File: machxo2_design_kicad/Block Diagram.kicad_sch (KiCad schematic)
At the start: 0 parts

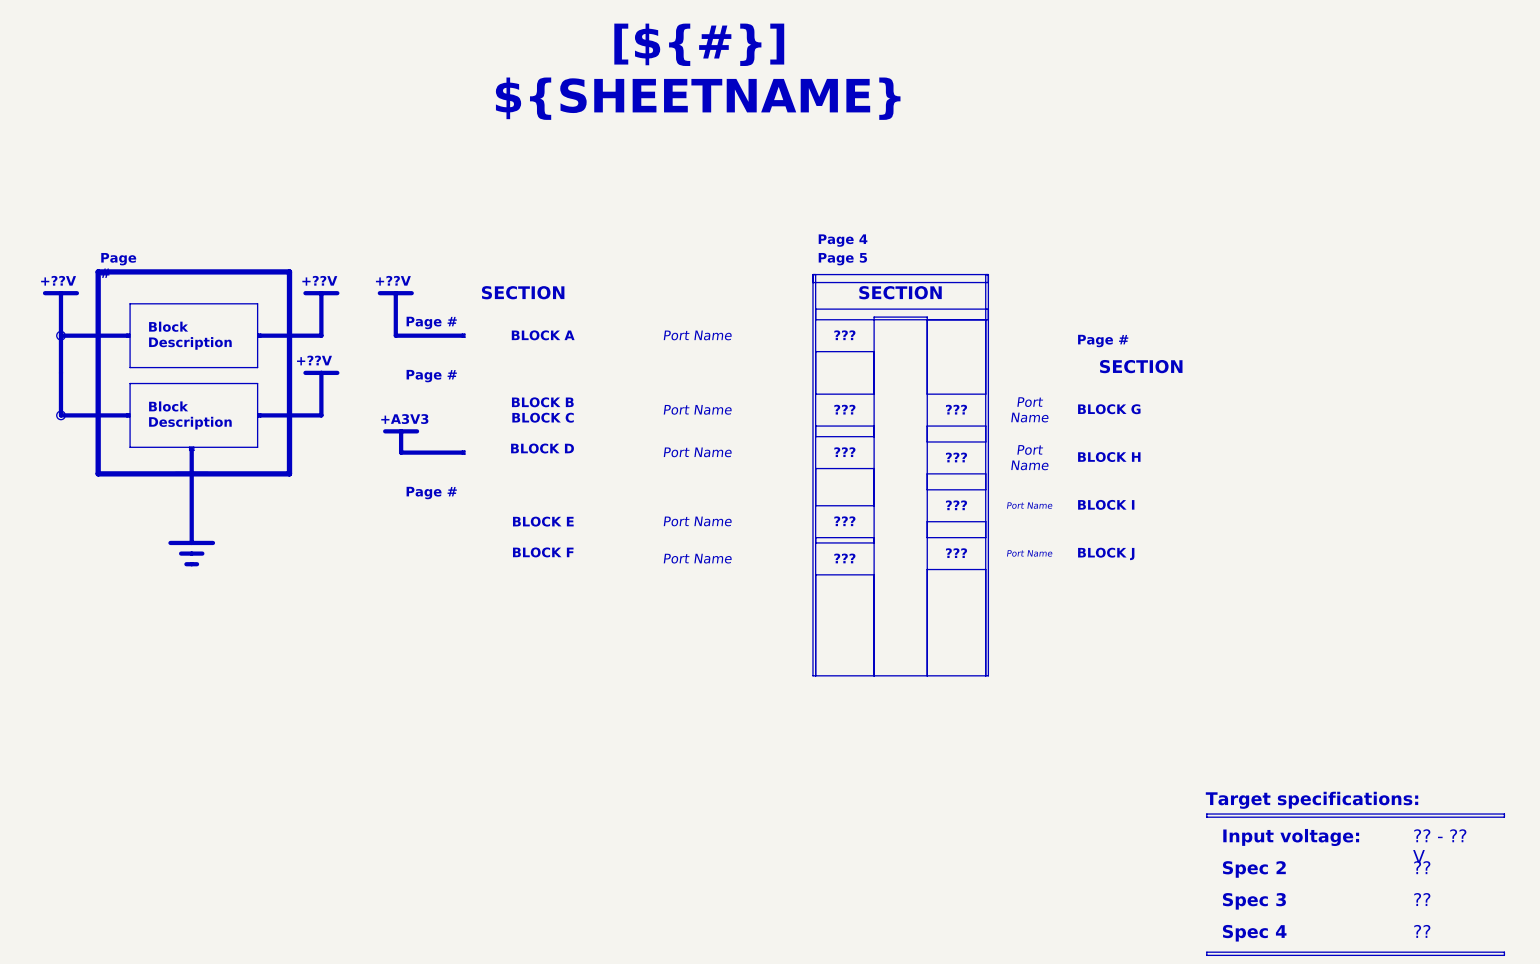
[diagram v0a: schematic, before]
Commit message: Prelimary schematic done. Need to create BOM and review.
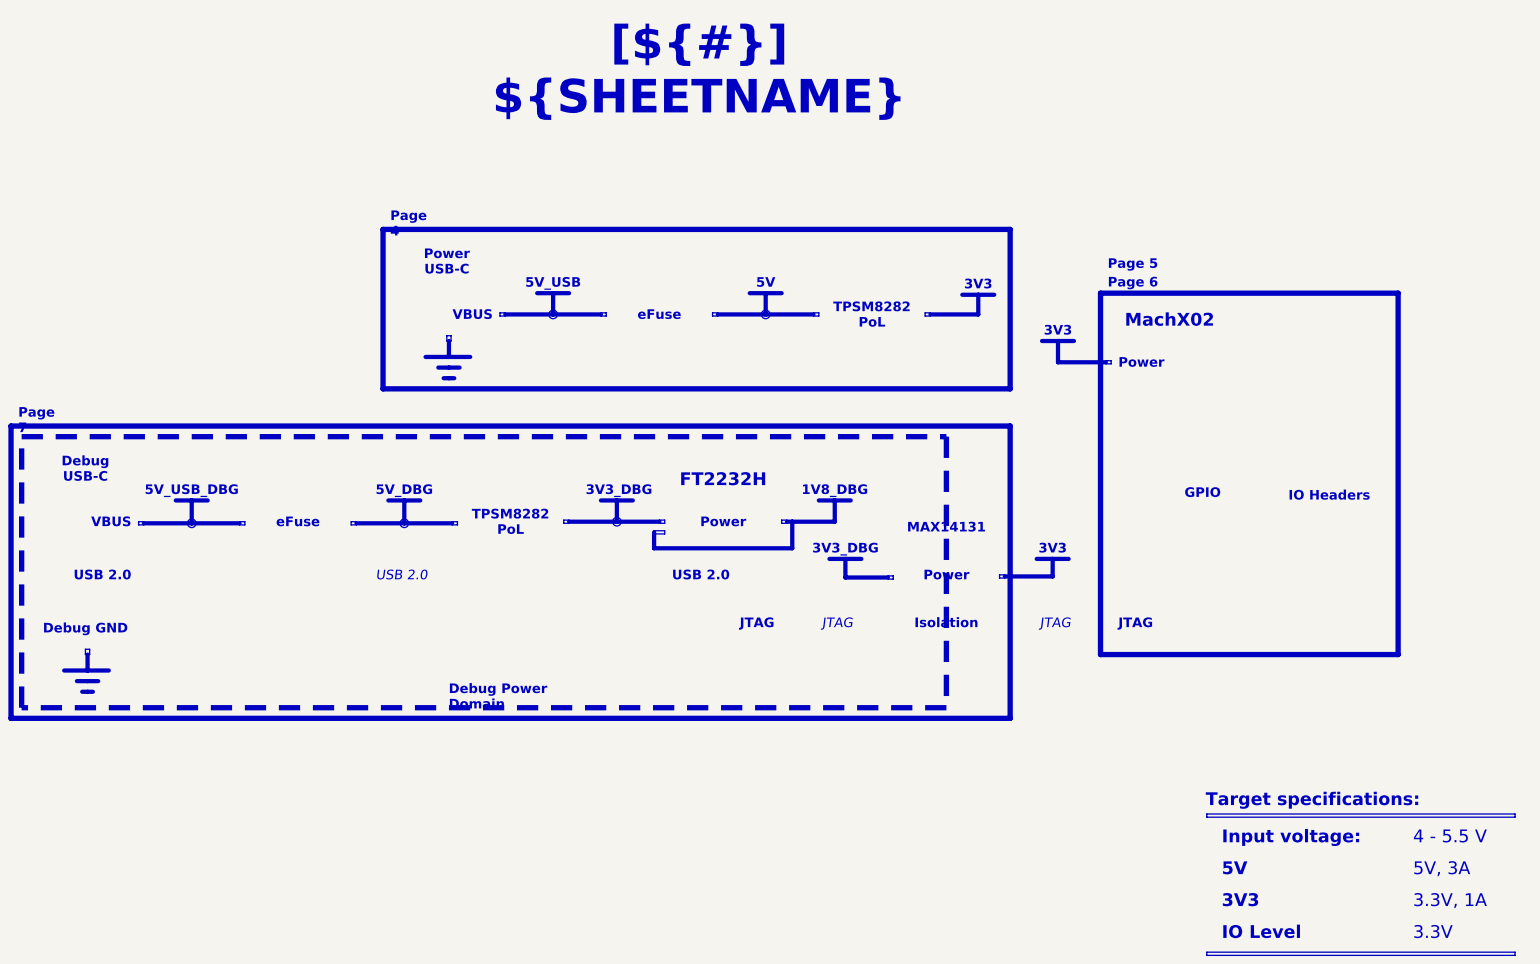
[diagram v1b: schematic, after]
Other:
- note added: "1V8_DBG"
- note added: "3V3"
- note added: "3V3_DBG"
- note added: "5V"
- note added: "5V_DBG"
- note added: "5V_USB"
- note added: "5V_USB_DBG"
- note removed: "+??V"
- note removed: "+A3V3"
